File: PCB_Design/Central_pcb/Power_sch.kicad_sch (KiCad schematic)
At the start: 16 parts, among them J2 Barrel_Jack, U2 BQ25171QWDRCRQ1, U3 AMS1117-3.3

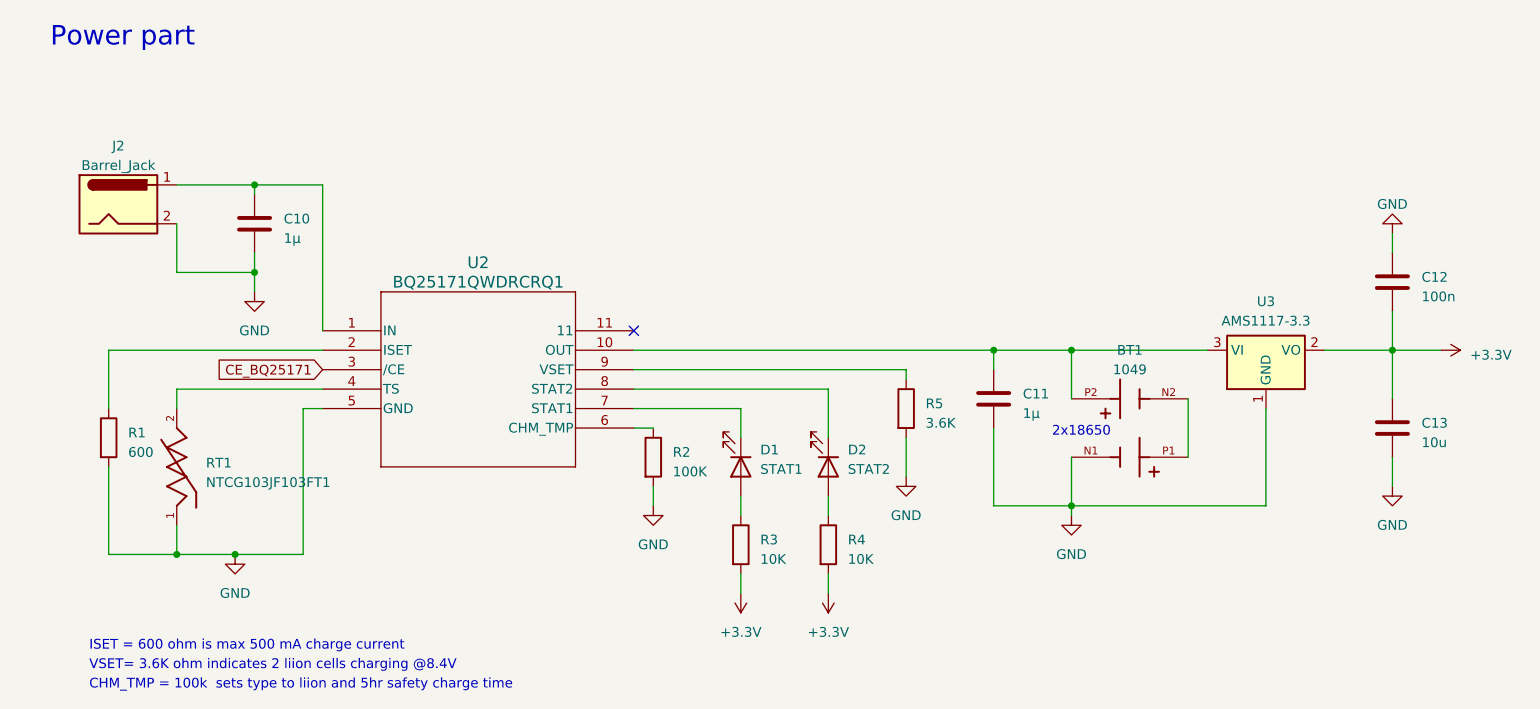
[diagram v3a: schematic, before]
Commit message: PCB route
Volledig geroute nog juist controleren en mounting holes doen + controleren dat er overal gnd en 3.3v mooi verbonden is
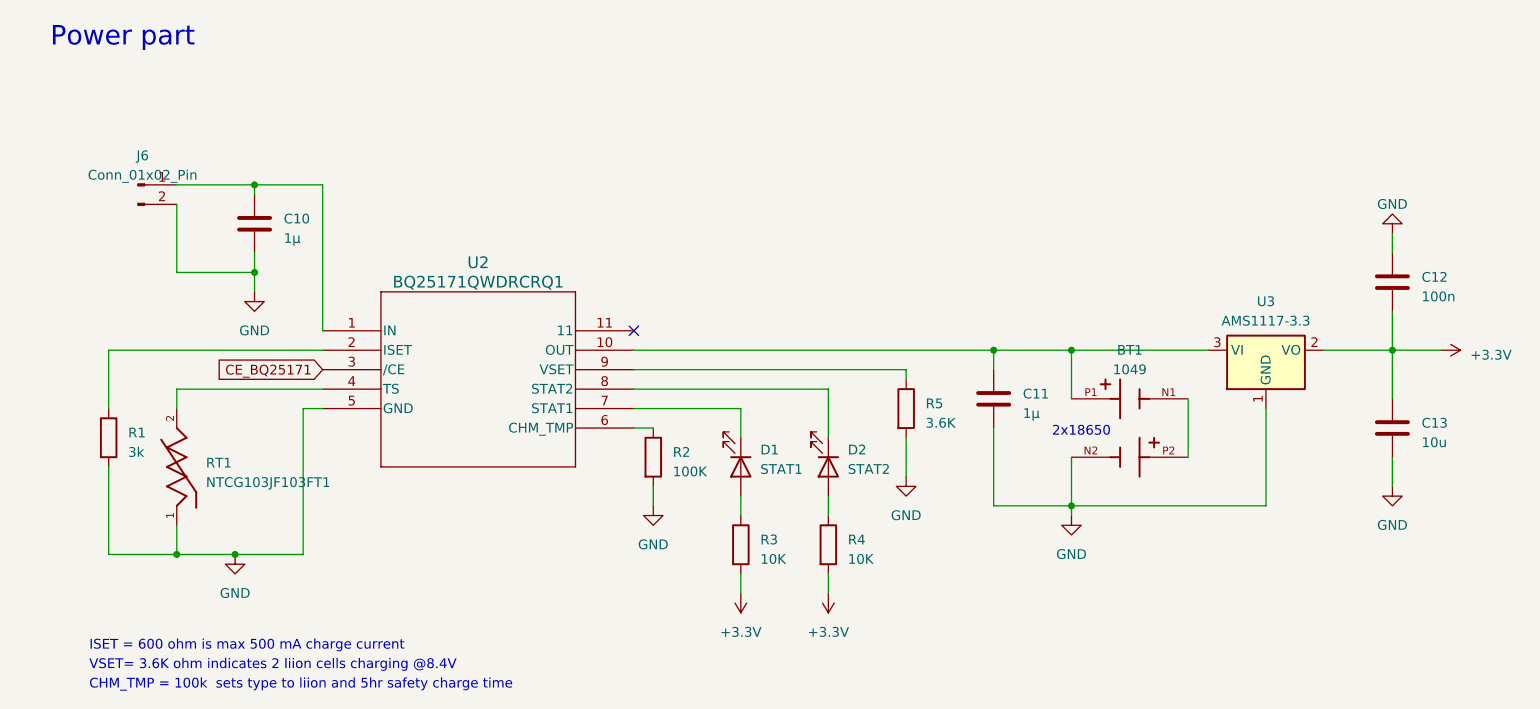
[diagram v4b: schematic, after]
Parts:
- removed J2: Barrel_Jack, Connector_BarrelJack:BarrelJack_GCT_DCJ200-10-A_Horizontal, symbol Connector:Barrel_Jack
- added J6: Conn_01x02_Pin, Connector_PinSocket_2.54mm:PinSocket_1x02_P2.54mm_Vertical, symbol Connector:Conn_01x02_Pin
- R1: value 600 -> 3k
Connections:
- net GND: now also BT1.N2, J6.2 (Pin_2); no longer BT1.N1
- net at C10.1, U2.1 (IN): now also J6.1 (Pin_1)
- net at BT1.P1: now also C11.1, U2.10 (OUT), U3.3 (VI); no longer BT1.N2
- new net: BT1.N1, BT1.P2
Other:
- moved on the sheet: BT1
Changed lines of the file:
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@@
     (stroke (width 0) (type default))
   )
-  (wire (pts (xy 93.98 63.5) (xy 93.98 57.15))
+  (wire (pts (xy 93.98 54.61) (xy 93.98 63.5))
     (stroke (width 0) (type default))
   )
@@
     (stroke (width 0) (type default))
   )
+  (wire (pts (xy 210.82 73.66) (xy 210.82 80.01))
+    (stroke (width 0) (type default))
+  )
   (wire (pts (xy 167.64 102.87) (xy 167.64 105.41))
-    (stroke (width 0) (type default))
-  )
-  (wire (pts (xy 210.82 73.66) (xy 210.82 80.01))
     (stroke (width 0) (type default))
   )
@@
     )
   )
-  (symbol (lib_id "Connector:Barrel_Jack") (at 86.36 54.61 0) (unit 1)
-    (in_bom yes) (on_board yes) (dnp no) (fields_autoplaced)
-    (property "Reference" "J2" (at 86.36 46.99 0)
-      (effects (font (size 1.27 1.27)))
-    )
-    (property "Value" "Barrel_Jack" (at 86.36 49.53 0)
-      (effects (font (size 1.27 1.27)))
-    )
-    (property "Footprint" "Connector_BarrelJack:BarrelJack_GCT_DCJ200-10-A_Horizontal" (at 87.63 55.626 0)
-      (effects (font (size 1.27 1.27)) hide)
-    )
-    (property "Datasheet" "~" (at 87.63 55.626 0)
-      (effects (font (size 1.27 1.27)) hide)
-    )
-    (pin "1")
-    (pin "2")
-    (instances
-      (project "Central_pcb"
-        (path "/4d244925-fc91-48ed-8daa-e4f0d6afeb7f/3414a10a-973a-4a85-bec5-f896220b0f20"
-          (reference "J2") (unit 1)
-        )
-      )
-    )
-  )
   (symbol (lib_id "Device:R") (at 85.09 85.09 0) (unit 1)
     (in_bom yes) (on_board yes) (dnp no) (fields_autoplaced)
@@
       (effects (font (size 1.27 1.27)) (justify left))
     )
-    (property "Value" "600" (at 87.63 86.995 0)
+    (property "Value" "3k" (at 87.63 86.995 0)
       (effects (font (size 1.27 1.27)) (justify left))
     )
@@
     )
   )
-  (symbol (lib_id "1049P:1049") (at 218.44 82.55 180) (unit 1)
+  (symbol (lib_id "1049P:1049") (at 218.44 85.09 0) (unit 1)
     (in_bom yes) (on_board yes) (dnp no) (fields_autoplaced)
     (property "Reference" "BT1" (at 218.44 73.66 0)
@@
       (effects (font (size 1.27 1.27)))
     )
-    (property "Footprint" "Central:BAT_1049" (at 218.44 82.55 0)
-      (effects (font (size 1.27 1.27)) (justify bottom) hide)
-    )
-    (property "Datasheet" "" (at 218.44 82.55 0)
-      (effects (font (size 1.27 1.27)) hide)
-    )
-    (property "MF" "Keystone Electronics" (at 218.44 82.55 0)
-      (effects (font (size 1.27 1.27)) (justify bottom) hide)
-    )
-    (property "MAXIMUM_PACKAGE_HEIGHT" "15.1mm" (at 218.44 82.55 0)
-      (effects (font (size 1.27 1.27)) (justify bottom) hide)
-    )
-    (property "Package" "None" (at 218.44 82.55 0)
-      (effects (font (size 1.27 1.27)) (justify bottom) hide)
-    )
-    (property "Price" "None" (at 218.44 82.55 0)
-      (effects (font (size 1.27 1.27)) (justify bottom) hide)
-    )
-    (property "Check_prices" "https://www.snapeda.com/parts/1049/Keystone+Electronics/view-part/?ref=eda" (at 218.44 82.55 0)
-      (effects (font (size 1.27 1.27)) (justify bottom) hide)
-    )
-    (property "STANDARD" "Manufacturer Recommendations" (at 218.44 82.55 0)
-      (effects (font (size 1.27 1.27)) (justify bottom) hide)
-    )
-    (property "PARTREV" "F" (at 218.44 82.55 0)
-      (effects (font (size 1.27 1.27)) (justify bottom) hide)
-    )
-    (property "SnapEDA_Link" "https://www.snapeda.com/parts/1049/Keystone+Electronics/view-part/?ref=snap" (at 218.44 82.55 0)
-      (effects (font (size 1.27 1.27)) (justify bottom) hide)
-    )
-    (property "MP" "1049" (at 218.44 82.55 0)
-      (effects (font (size 1.27 1.27)) (justify bottom) hide)
-    )
-    (property "Description" "\nTHM Holder for Dual 18650 Batteries\n" (at 218.44 82.55 0)
-      (effects (font (size 1.27 1.27)) (justify bottom) hide)
-    )
-    (property "MANUFACTURER" "Keystone" (at 218.44 82.55 0)
-      (effects (font (size 1.27 1.27)) (justify bottom) hide)
-    )
-    (property "Availability" "Not in stock" (at 218.44 82.55 0)
-      (effects (font (size 1.27 1.27)) (justify bottom) hide)
-    )
-    (property "SNAPEDA_PN" "109" (at 218.44 82.55 0)
+    (property "Footprint" "Central:BAT_1049" (at 218.44 85.09 0)
+      (effects (font (size 1.27 1.27)) (justify bottom) hide)
+    )
+    (property "Datasheet" "" (at 218.44 85.09 0)
+      (effects (font (size 1.27 1.27)) hide)
+    )
+    (property "MF" "Keystone Electronics" (at 218.44 85.09 0)
+      (effects (font (size 1.27 1.27)) (justify bottom) hide)
+    )
+    (property "MAXIMUM_PACKAGE_HEIGHT" "15.1mm" (at 218.44 85.09 0)
+      (effects (font (size 1.27 1.27)) (justify bottom) hide)
+    )
+    (property "Package" "None" (at 218.44 85.09 0)
+      (effects (font (size 1.27 1.27)) (justify bottom) hide)
+    )
+    (property "Price" "None" (at 218.44 85.09 0)
+      (effects (font (size 1.27 1.27)) (justify bottom) hide)
+    )
+    (property "Check_prices" "https://www.snapeda.com/parts/1049/Keystone+Electronics/view-part/?ref=eda" (at 218.44 85.09 0)
+      (effects (font (size 1.27 1.27)) (justify bottom) hide)
+    )
+    (property "STANDARD" "Manufacturer Recommendations" (at 218.44 85.09 0)
+      (effects (font (size 1.27 1.27)) (justify bottom) hide)
+    )
+    (property "PARTREV" "F" (at 218.44 85.09 0)
+      (effects (font (size 1.27 1.27)) (justify bottom) hide)
+    )
+    (property "SnapEDA_Link" "https://www.snapeda.com/parts/1049/Keystone+Electronics/view-part/?ref=snap" (at 218.44 85.09 0)
+      (effects (font (size 1.27 1.27)) (justify bottom) hide)
+    )
+    (property "MP" "1049" (at 218.44 85.09 0)
+      (effects (font (size 1.27 1.27)) (justify bottom) hide)
+    )
+    (property "Description" "\nTHM Holder for Dual 18650 Batteries\n" (at 218.44 85.09 0)
+      (effects (font (size 1.27 1.27)) (justify bottom) hide)
+    )
+    (property "MANUFACTURER" "Keystone" (at 218.44 85.09 0)
+      (effects (font (size 1.27 1.27)) (justify bottom) hide)
+    )
+    (property "Availability" "Not in stock" (at 218.44 85.09 0)
+      (effects (font (size 1.27 1.27)) (justify bottom) hide)
+    )
+    (property "SNAPEDA_PN" "109" (at 218.44 85.09 0)
       (effects (font (size 1.27 1.27)) (justify bottom) hide)
     )
@@
         )
       )
+    )
+  )
+  (symbol (lib_id "Connector:Conn_01x02_Pin") (at 88.9 52.07 0) (unit 1)
+    (in_bom yes) (on_board yes) (dnp no) (fields_autoplaced)
+    (property "Reference" "J6" (at 89.535 48.26 0)
+      (effects (font (size 1.27 1.27)))
+    )
+    (property "Value" "Conn_01x02_Pin" (at 89.535 50.8 0)
+      (effects (font (size 1.27 1.27)))
+    )
+    (property "Footprint" "Connector_PinSocket_2.54mm:PinSocket_1x02_P2.54mm_Vertical" (at 88.9 52.07 0)
+      (effects (font (size 1.27 1.27)) hide)
+    )
+    (property "Datasheet" "~" (at 88.9 52.07 0)
+      (effects (font (size 1.27 1.27)) hide)
+    )
+    (pin "1")
+    (pin "2")
+    (instances
+      (project "Central_pcb"
+        (path "/4d244925-fc91-48ed-8daa-e4f0d6afeb7f/3414a10a-973a-4a85-bec5-f896220b0f20"
+          (reference "J6") (unit 1)
+        )
+      )
